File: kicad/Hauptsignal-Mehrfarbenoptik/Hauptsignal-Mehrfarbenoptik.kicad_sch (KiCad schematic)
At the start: 17 parts, among them J0 VCC, J1 VkzBw, J2 ARGB_2, J3 ARGB_3, J4 ARGB_4, J5 Zs7-3, J6 Ra, J7 Zs7-1, J8 Zs7-2, J9 Ra/Zs1

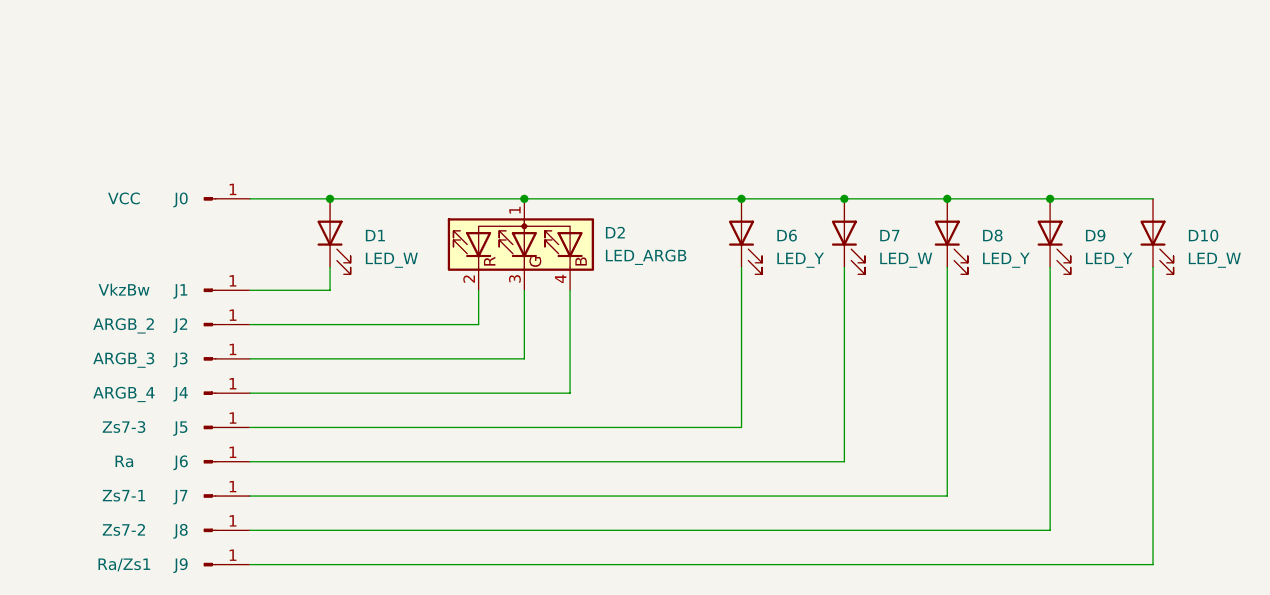
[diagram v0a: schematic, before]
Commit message: feat: re-route MSO
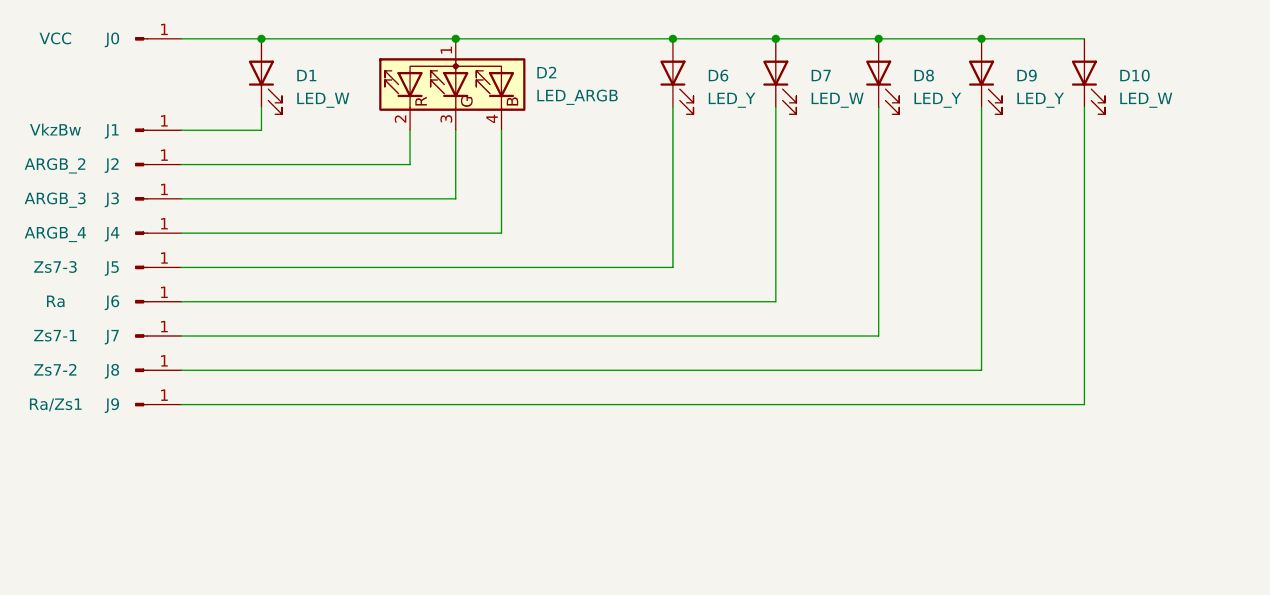
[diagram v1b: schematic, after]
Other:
- title: (none) -> KS-Signalschirm für mehrfarbige Optik
- moved on the sheet: D1, D10, D2, D6, D7, D8, D9, J0, J1, J2, J3, J4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
